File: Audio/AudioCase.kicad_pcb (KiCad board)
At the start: 2 copper layers, 271 x 112.8 mm, 87 parts, among them J10 AMP_AUX_IN, J11 AMP_AUX_OUT, J4 PWR_IN, J5 PWR_OUT, J6 AUX_IN, J7 V_IN, J8 AUX_OUT, J9 AMP_PWR, U3 NJM4558, U4 NJM4558

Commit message: Audio: Controll端子・リレー配線とPCB部品配置まで反映。
ControllにAmp向け2P端子10個とリレー周りの回路を更新し、AudioCaseへフットプリントを配置。EQ/Amp/Controllは回路図レイアウトに合わせて部品位置を調整（PowerModuleは配線済みのため未変更）。BP5293-50フットプリント修正と配置用スクリプトを追加。

Co-authored-by: Cursor <cursoragent@cursor.com>
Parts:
- removed C30: 0.1μF, Capacitor_THT:C_Rect_L7.2mm_W2.5mm_P5.00mm_FKS2_FKP2_MKS2_MKP2
- removed C31: 10μF, Capacitor_THT:CP_Radial_D5.0mm_P2.00mm
- removed C32, C33: 470μF, Capacitor_THT:CP_Radial_D16.0mm_P7.50mm
- removed F2: 1A, Resistor_THT:R_Axial_DIN0411_L9.9mm_D3.6mm_P12.70mm_Horizontal
- added A1: RaspberryPi_Pico, Module:RaspberryPi_Pico_Common_Unspecified, F.Cu at (100.8, 150.2)
- added C1: 47μF, Capacitor_THT:CP_Radial_D8.0mm_P3.50mm, F.Cu at (227.8, 39.2)
- added C2: 4.7μF, Capacitor_THT:CP_Radial_D5.0mm_P2.00mm, F.Cu at (256.0, 25.2)
- added C3: 4.7μF, Capacitor_THT:CP_Radial_D5.0mm_P2.00mm, F.Cu at (256.2, 45.7)
- added C4: 0.1μF, Capacitor_SMD:C_1206_3216Metric_Pad1.33x1.80mm_HandSolder, F.Cu at (256.0, 31.5)
- added F1: 1A, Resistor_THT:R_Axial_DIN0411_L9.9mm_D3.6mm_P12.70mm_Horizontal, F.Cu at (220.0, 33.4)
- added H13: MountingHole, MountingHole:MountingHole_3.2mm_M3, F.Cu at (21.2, 159.7)
- added H14: MountingHole, MountingHole:MountingHole_3.2mm_M3, F.Cu at (21.2, 167.7)
- added H15: MountingHole, MountingHole:MountingHole_3.2mm_M3, F.Cu at (21.2, 175.6)
- added H16: MountingHole, MountingHole:MountingHole_3.2mm_M3, F.Cu at (21.2, 183.6)
- added J12: AMP1_PWR, TerminalBlock_Phoenix:TerminalBlock_Phoenix_MKDS-1,5-2-5.08_1x02_P5.08mm_Horizontal, F.Cu at (60.8, 68.6)
- added J13: AMP1_PWR, TerminalBlock_Phoenix:TerminalBlock_Phoenix_MKDS-1,5-2-5.08_1x02_P5.08mm_Horizontal, F.Cu at (68.4, 119.2)
- added J14: AMP1_PWR, TerminalBlock_Phoenix:TerminalBlock_Phoenix_MKDS-1,5-2-5.08_1x02_P5.08mm_Horizontal, F.Cu at (68.9, 127.3)
- added J15: AMP1_LR, TerminalBlock_Phoenix:TerminalBlock_Phoenix_MKDS-1,5-2-5.08_1x02_P5.08mm_Horizontal, F.Cu at (80.3, 70.3)
- added J16: AMP2_PWR, TerminalBlock_Phoenix:TerminalBlock_Phoenix_MKDS-1,5-2-5.08_1x02_P5.08mm_Horizontal, F.Cu at (102.6, 68.6)
- added J17: AMP2_LR, TerminalBlock_Phoenix:TerminalBlock_Phoenix_MKDS-1,5-2-5.08_1x02_P5.08mm_Horizontal, F.Cu at (122.7, 70.3)
- added J18: AMP3_PWR, TerminalBlock_Phoenix:TerminalBlock_Phoenix_MKDS-1,5-2-5.08_1x02_P5.08mm_Horizontal, F.Cu at (142.3, 69.2)
- added J19: AMP4_PWR, TerminalBlock_Phoenix:TerminalBlock_Phoenix_MKDS-1,5-2-5.08_1x02_P5.08mm_Horizontal, F.Cu at (142.8, 85.0)
- added J20: AMP5_PWR, TerminalBlock_Phoenix:TerminalBlock_Phoenix_MKDS-1,5-2-5.08_1x02_P5.08mm_Horizontal, F.Cu at (143.9, 101.8)
- added J21: AMP3_PWR, TerminalBlock_Phoenix:TerminalBlock_Phoenix_MKDS-1,5-2-5.08_1x02_P5.08mm_Horizontal, F.Cu at (162.4, 70.8)
- added J22: AMP4_PWR, TerminalBlock_Phoenix:TerminalBlock_Phoenix_MKDS-1,5-2-5.08_1x02_P5.08mm_Horizontal, F.Cu at (163.5, 86.6)
- added J23: AMP5_PWR, TerminalBlock_Phoenix:TerminalBlock_Phoenix_MKDS-1,5-2-5.08_1x02_P5.08mm_Horizontal, F.Cu at (164.0, 103.4)
- added J24: OLED_PIN, TerminalBlock_Phoenix:TerminalBlock_Phoenix_MKDS-1,5-4-5.08_1x04_P5.08mm_Horizontal, F.Cu at (73.3, 98.0)
- added K1: AZ850P2-x, Relay_THT:Relay_DPDT_FRT5, F.Cu at (67.3, 72.5)
- added K10: AZ850P2-x, Relay_THT:Relay_DPDT_FRT5, F.Cu at (167.5, 113.8)
- added K2: AZ850P2-x, Relay_THT:Relay_DPDT_FRT5, F.Cu at (87.4, 74.1)
- added K3: AZ850P2-x, Relay_THT:Relay_DPDT_FRT5, F.Cu at (109.1, 72.5)
- added K4: AZ850P2-x, Relay_THT:Relay_DPDT_FRT5, F.Cu at (129.2, 74.1)
- added K5: AZ850P2-x, Relay_THT:Relay_DPDT_FRT5, F.Cu at (148.8, 73.0)
- added K6: AZ850P2-x, Relay_THT:Relay_DPDT_FRT5, F.Cu at (149.4, 88.8)
- added K7: AZ850P2-x, Relay_THT:Relay_DPDT_FRT5, F.Cu at (150.4, 105.6)
- added K8: AZ850P2-x, Relay_THT:Relay_DPDT_FRT5, F.Cu at (168.9, 74.6)
- added K9: AZ850P2-x, Relay_THT:Relay_DPDT_FRT5, F.Cu at (169.5, 90.4)
- added NT1: NetTie_2, NetTie:NetTie-2_THT_Pad1.0mm, F.Cu at (62.9, 121.4)
- added SW1: RotaryEncoder_Switch, Rotary_Encoder:RotaryEncoder_Alps_EC11E-Switch_Vertical_H20mm, F.Cu at (62.4, 104.0)
- added U1: MCW03, Library:MCW03-12D15_SIP7_THT, F.Cu at (225.9, 54.9)
- added U5: ULN2803A, Library:ULN2803A_DIP-18_W7.62mm, F.Cu at (124.4, 93.1)
- added U6: ULN2803A, Library:ULN2803A_DIP-18_W7.62mm, F.Cu at (124.9, 111.0)
- added U7: ULN2803A, Library:ULN2803A_DIP-18_W7.62mm, F.Cu at (124.9, 125.7)
- C10, C15: value 0.047μF -> 0.01uF; footprint Capacitor_THT:C_Rect_L7.2mm_W3.5mm_P5.00mm_FKS2_FKP2_MKS2_MKP2 -> Capacitor_THT:C_Rect_L7.2mm_W3.0mm_P5.00mm_FKS2_FKP2_MKS2_MKP2
- C11: value 0.01uF -> 0.047μF; footprint Capacitor_THT:C_Rect_L7.2mm_W3.0mm_P5.00mm_FKS2_FKP2_MKS2_MKP2 -> Capacitor_THT:C_Rect_L7.2mm_W3.5mm_P5.00mm_FKS2_FKP2_MKS2_MKP2
- C13: value 2200pF -> 0.01uF; footprint Capacitor_THT:C_Rect_L7.2mm_W4.5mm_P5.00mm_FKS2_FKP2_MKS2_MKP2 -> Capacitor_THT:C_Rect_L7.2mm_W3.0mm_P5.00mm_FKS2_FKP2_MKS2_MKP2
- C14, C17: value 0.01uF -> 2200pF; footprint Capacitor_THT:C_Rect_L7.2mm_W3.0mm_P5.00mm_FKS2_FKP2_MKS2_MKP2 -> Capacitor_THT:C_Rect_L7.2mm_W4.5mm_P5.00mm_FKS2_FKP2_MKS2_MKP2
- C16: value 0.047μF -> 2200pF; footprint Capacitor_THT:C_Rect_L7.2mm_W3.5mm_P5.00mm_FKS2_FKP2_MKS2_MKP2 -> Capacitor_THT:C_Rect_L7.2mm_W4.5mm_P5.00mm_FKS2_FKP2_MKS2_MKP2
- C18, C20, C21: value 2200pF -> 0.1μF; footprint Capacitor_THT:C_Rect_L7.2mm_W4.5mm_P5.00mm_FKS2_FKP2_MKS2_MKP2 -> Capacitor_SMD:C_1206_3216Metric_Pad1.33x1.80mm_HandSolder
- C19: value 0.01uF -> 0.1μF; footprint Capacitor_THT:C_Rect_L7.2mm_W3.0mm_P5.00mm_FKS2_FKP2_MKS2_MKP2 -> Capacitor_SMD:C_1206_3216Metric_Pad1.33x1.80mm_HandSolder
- C22, C23: footprint Capacitor_SMD:C_1206_3216Metric_Pad1.33x1.80mm_HandSolder -> Resistor_SMD:R_0603_1608Metric_Pad0.98x0.95mm_HandSolder
- C24, C26: footprint Capacitor_SMD:C_1206_3216Metric_Pad1.33x1.80mm_HandSolder -> Capacitor_THT:C_Rect_L7.2mm_W2.5mm_P5.00mm_FKS2_FKP2_MKS2_MKP2
- C25, C27: value 0.1μF -> 10μF; footprint Capacitor_SMD:C_1206_3216Metric_Pad1.33x1.80mm_HandSolder -> Capacitor_THT:CP_Radial_D5.0mm_P2.00mm
- C28: value 0.1μF -> 470μF; footprint Capacitor_THT:C_Rect_L7.2mm_W2.5mm_P5.00mm_FKS2_FKP2_MKS2_MKP2 -> Capacitor_THT:CP_Radial_D16.0mm_P7.50mm
- C29: value 10μF -> 470μF; footprint Capacitor_THT:CP_Radial_D5.0mm_P2.00mm -> Capacitor_THT:CP_Radial_D16.0mm_P7.50mm
- C5: value 47μF -> 0.1μF; footprint Capacitor_THT:CP_Radial_D8.0mm_P3.50mm -> Capacitor_SMD:C_1206_3216Metric_Pad1.33x1.80mm_HandSolder
- C6: value 4.7μF -> 0.047μF; footprint Capacitor_THT:CP_Radial_D5.0mm_P2.00mm -> Capacitor_THT:C_Rect_L7.2mm_W3.5mm_P5.00mm_FKS2_FKP2_MKS2_MKP2
- C7: value 4.7μF -> 0.01uF; footprint Capacitor_THT:CP_Radial_D5.0mm_P2.00mm -> Capacitor_THT:C_Rect_L7.2mm_W3.0mm_P5.00mm_FKS2_FKP2_MKS2_MKP2
- C8: value 0.1μF -> 0.047μF; footprint Capacitor_SMD:C_1206_3216Metric_Pad1.33x1.80mm_HandSolder -> Capacitor_THT:C_Rect_L7.2mm_W3.5mm_P5.00mm_FKS2_FKP2_MKS2_MKP2
- C9: value 0.1μF -> 2200pF; footprint Capacitor_SMD:C_1206_3216Metric_Pad1.33x1.80mm_HandSolder -> Capacitor_THT:C_Rect_L7.2mm_W4.5mm_P5.00mm_FKS2_FKP2_MKS2_MKP2
- R19, R20, R21, R22, R23, R24, R25, R26, R27, R28: footprint Resistor_SMD:R_1206_3216Metric_Pad1.30x1.75mm_HandSolder -> Resistor_SMD:R_0603_1608Metric_Pad0.98x0.95mm_HandSolder
- U2: value ~ -> NJM4558; footprint Library:MCW03-12D15_SIP7_THT -> Package_DIP:DIP-8_W7.62mm_Socket
- U4: value NJM4558 -> BP5293-50; footprint Package_DIP:DIP-8_W7.62mm_Socket -> BP5293_ROHM:BP5293-50_ROHM_SIP-3
- moved J9 263.2 mm to (265.7, 80.5), turned to 180 degrees
- moved C20 256.0 mm to (265.6, 94.0)
- moved H9 255.6 mm to (266.5, 141.8)
- moved H10 255.5 mm to (266.5, 146.4)
- moved H11 255.3 mm to (266.5, 151.1)
- moved H12 255.2 mm to (266.5, 155.8)
- moved C21 252.8 mm to (265.6, 108.0)
- moved C26 251.4 mm to (208.8, 148.5)
- moved C18 248.5 mm to (249.2, 94.0)
- moved C6 245.0 mm to (11.1, 22.7)
- moved C19 244.9 mm to (249.2, 108.0)
- moved C9 241.6 mm to (23.9, 105.7)
- moved C7 241.1 mm to (15.7, 65.9)
- moved C27 239.8 mm to (208.8, 156.7)
- moved C8 234.6 mm to (21.6, 22.7)
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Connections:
- AMP1 pad 4: /AmpModule/V-_IN -> /Controll/AMP_V-_OUT
- AMP1 pad 8: /AmpModule/V+_IN -> /Controll/AMP_V+_OUT
- C12 pad 1: Net-(C10-Pad2) -> Net-(C11-Pad2)
- C14 pad 1: Net-(C11-Pad2) -> Net-(C14-Pad1)
- C15 pad 1: Net-(C15-Pad1) -> Net-(C13-Pad2)
- C16 pad 1: Net-(C15-Pad2) -> Net-(C16-Pad1)
- C17 pad 1: Net-(C17-Pad1) -> Net-(C16-Pad2)
- C18 pad 1: Net-(C13-Pad2) -> /Controll/AMP_V+_IN
- C18 pad 2: Net-(C18-Pad2) -> GND
- C19 pad 1: Net-(C17-Pad2) -> GND
- C19 pad 2: Net-(C19-Pad2) -> /Controll/AMP_V-_IN
- C20 pad 1: Net-(C20-Pad1) -> /Controll/AMP_V+_IN
- C20 pad 2: Net-(C20-Pad2) -> GND
- C21 pad 1: Net-(C20-Pad2) -> GND
- C21 pad 2: Net-(C21-Pad2) -> /Controll/AMP_V-_IN
- C22 pad 1: /Controll/AMP_V+_IN -> GND
- C22 pad 2: GND -> /Controll/AMP_V+_OUT
- C23 pad 1: GND -> /Controll/AMP_V-_OUT
- C23 pad 2: /Controll/AMP_V-_IN -> GND
- C24 pad 1: /Controll/AMP_V+_IN -> Net-(AMP1A-+)
- C24 pad 2: GND -> /Controll/R_OUT
- C25 pad 1: GND -> Net-(AMP1A-+)
- C25 pad 2: /Controll/AMP_V-_IN -> /Controll/R_OUT
- C26 pad 1: GND -> Net-(AMP1B-+)
- C26 pad 2: /AmpModule/V+_IN -> /Controll/L_OUT
- C27 pad 1: /AmpModule/V-_IN -> Net-(AMP1B-+)
- C27 pad 2: GND -> /Controll/L_OUT
- C28 pad 1: Net-(AMP1A-+) -> Net-(C28-Pad1)
- C28 pad 2: /AmpModule/R_IN -> /AmpModule/R_OUT
- C29 pad 1: Net-(AMP1A-+) -> Net-(C29-Pad1)
- C29 pad 2: /AmpModule/R_IN -> /AmpModule/L_OUT
- C5 pad 1: Net-(U2-+Vin) -> GND
- C5 pad 2: /Controll/5VGND_CTRL -> /Controll/AMP_V-_IN
- C6 pad 1: /Controll/AMP_V+_IN -> Net-(C6-Pad1)
- C6 pad 2: GND -> Net-(C6-Pad2)
- C7 pad 1: GND -> Net-(C7-Pad1)
- C7 pad 2: /Controll/AMP_V-_IN -> Net-(C10-Pad1)
- C8 pad 1: /Controll/AMP_V+_IN -> Net-(C6-Pad2)
- C8 pad 2: GND -> Net-(C8-Pad2)
- C9 pad 1: GND -> Net-(C9-Pad1)
- C9 pad 2: /Controll/AMP_V-_IN -> Net-(C14-Pad1)
- J10 pad 1: /AmpModule/R_IN -> /Controll/R_OUT
- J10 pad 2: /AmpModule/L_IN -> /Controll/L_OUT
- J4 pad 1: /Controll/5VGND_CTRL -> /Controll/PD_GND_IN
- J4 pad 2: /PowerModule/+15_IN -> /Controll/+15_IN
- J9 pad 1: /AmpModule/V+_IN -> /Controll/AMP_V+_OUT
- J9 pad 3: /AmpModule/V-_IN -> /Controll/AMP_V-_OUT
- L1 pad 2: Net-(U2-+Vout) -> Net-(U1-+Vout)
- L2 pad 1: Net-(U2--Vout) -> Net-(U1--Vout)
- R1 pad 2: Net-(C10-Pad1) -> Net-(C6-Pad1)
- R10 pad 1: Net-(C15-Pad1) -> Net-(C11-Pad1)
- R11 pad 1: Net-(C17-Pad1) -> Net-(C13-Pad1)
- R12 pad 1: Net-(C20-Pad1) -> Net-(C16-Pad1)
- R15 pad 1: Net-(U4A--) -> Net-(U3A--)
- R16 pad 1: Net-(U4B--) -> Net-(U3B--)
- R17 pad 2: Net-(U4A--) -> Net-(U3A--)
- R18 pad 2: Net-(U4B--) -> Net-(U3B--)
- R19 pad 1: /AmpModule/R_IN -> /Controll/R_OUT
- R2 pad 2: Net-(C11-Pad1) -> Net-(C7-Pad1)
- R20 pad 1: /AmpModule/L_IN -> /Controll/L_OUT
- R27 pad 2: Net-(C32-Pad1) -> Net-(C28-Pad1)
- R28 pad 2: Net-(C33-Pad1) -> Net-(C29-Pad1)
- R3 pad 1: Net-(C10-Pad2) -> Net-(C6-Pad2)
- R4 pad 2: Net-(C13-Pad1) -> Net-(C9-Pad1)
- R5 pad 1: Net-(C16-Pad2) -> Net-(C12-Pad2)
- R6 pad 1: Net-(C11-Pad2) -> Net-(C10-Pad1)
- R7 pad 1: Net-(C19-Pad2) -> Net-(C15-Pad2)
- R8 pad 1: Net-(C13-Pad2) -> Net-(C14-Pad1)
- R9 pad 1: Net-(C21-Pad2) -> Net-(C17-Pad2)
- RV1 pad 1: Net-(C10-Pad1) -> Net-(C6-Pad1)
- RV1 pad 2: Net-(C10-Pad2) -> Net-(C6-Pad2)
- RV1 pad 3: Net-(C12-Pad2) -> Net-(C8-Pad2)
- RV1 pad 4: Net-(C16-Pad2) -> Net-(C12-Pad2)
- RV1 pad 5: Net-(C15-Pad2) -> Net-(C11-Pad2)
- RV1 pad 6: Net-(C15-Pad1) -> Net-(C11-Pad1)
- RV2 pad 1: Net-(C11-Pad1) -> Net-(C7-Pad1)
- RV2 pad 2: Net-(C11-Pad2) -> Net-(C10-Pad1)
- RV2 pad 3: Net-(C14-Pad2) -> Net-(C10-Pad2)
- RV2 pad 4: Net-(C19-Pad2) -> Net-(C15-Pad2)
- RV2 pad 5: Net-(C17-Pad2) -> Net-(C13-Pad2)
- RV2 pad 6: Net-(C17-Pad1) -> Net-(C13-Pad1)
- RV3 pad 1: Net-(C13-Pad1) -> Net-(C9-Pad1)
- RV3 pad 2: Net-(C13-Pad2) -> Net-(C14-Pad1)
- RV3 pad 3: Net-(C18-Pad2) -> Net-(C14-Pad2)
- RV3 pad 4: Net-(C21-Pad2) -> Net-(C17-Pad2)
- RV3 pad 5: Net-(C20-Pad2) -> Net-(C16-Pad2)
- RV3 pad 6: Net-(C20-Pad1) -> Net-(C16-Pad1)
- U2 pad 1: /Controll/5VGND_CTRL -> Net-(R13-Pad1)
- U2 pad 2: Net-(U2-+Vin) -> /EQModule/R BAX OUT
- U2 pad 3: unconnected-(U2-Remote_On/Off-Pad3) -> GND
- U2 pad 5: unconnected-(U2-NC-Pad5) -> GND
- U2 pad 6: Net-(U2-+Vout) -> /EQModule/L BAX OUT
- U2 pad 7: GND -> Net-(R14-Pad1)
- U2 pad 8: Net-(U2--Vout) -> /Controll/AMP_V+_IN
- U3 pad 1: Net-(R13-Pad1) -> /Controll/R_IN
- U3 pad 2: /EQModule/R BAX OUT -> Net-(U3A--)
- U3 pad 6: /EQModule/L BAX OUT -> Net-(U3B--)
- U3 pad 7: Net-(R14-Pad1) -> /Controll/L_IN
- U4 pad 1: /Controll/R_IN -> Net-(U4-VIN)
- U4 pad 2: Net-(U4A--) -> /Controll/CTRL_GND
- U4 pad 3: GND -> /Controll/5V_+
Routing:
- net Net-(U2-+Vin): track 37.9 -> 0.00 mm
- net /Controll/PD_GND_IN: track 0.00 -> 31.4 mm
- net /Controll/5VGND_CTRL: track 31.2 -> 0.00 mm
- net Net-(U1-+Vout): track 0.00 -> 30.8 mm
- net Net-(U2-+Vout): track 30.8 -> 0.00 mm
- net Net-(U1-+Vin): track 0.00 -> 26.6 mm
- net Net-(U2--Vout): track 17.6 -> 0.00 mm
- net Net-(U1--Vout): track 0.00 -> 14.1 mm
- net /PowerModule/+15_IN: track 11.0 -> 0.00 mm
- net /Controll/+15_IN: track 0.00 -> 9.99 mm
- net (no net): track 0.00 -> 3.50 mm
- net /Controll/AMP_V+_IN: track 55.2 -> 53.6 mm
- net /Controll/AMP_V-_IN: track 37.0 -> 36.4 mm
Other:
- board size 271 x 112.8 mm -> 277.5 x 115.3 mm

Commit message: Update audio KiCad project wiring.
Co-authored-by: Cursor <cursoragent@cursor.com>
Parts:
- added C30: 47μF, Capacitor_THT:CP_Radial_D8.0mm_P3.50mm, F.Cu at (194.3, 125.8)
- added C31: 0.1μF, Capacitor_THT:C_Disc_D5.0mm_W2.5mm_P2.50mm, F.Cu at (193.8, 133.4)
- added C32: 100μF, Capacitor_THT:CP_Radial_D6.3mm_P2.50mm, F.Cu at (195.3, 158.6)
- added C33: 0.1μF, Capacitor_THT:C_Disc_D5.0mm_W2.5mm_P2.50mm, F.Cu at (195.3, 151.8)
- added F2: 1A, Resistor_THT:R_Axial_DIN0411_L9.9mm_D3.6mm_P12.70mm_Horizontal, F.Cu at (186.2, 117.4)
- C19, C22, C23, R17, R19, R20, R21, R22, R23, R24: moved to B.Cu
- J13: value AMP1_PWR -> PD_IN
- J14: value AMP1_PWR -> AUDIO_IN
- J21: value AMP3_PWR -> AMP3_LR
- J22: value AMP4_PWR -> AMP4_LR
- J23: value AMP5_PWR -> AMP5_LR
- J24: footprint TerminalBlock_Phoenix:TerminalBlock_Phoenix_MKDS-1,5-4-5.08_1x04_P5.08mm_Horizontal -> Connector_PinHeader_2.54mm:PinHeader_1x04_P2.54mm_Vertical
- moved H7 197.4 mm to (168.2, 68.6)
- moved H6 184.5 mm to (168.2, 22.4)
- moved RV3 150.9 mm to (144.0, 65.8), turned to 90 degrees
- moved C19 149.4 mm to (118.2, 36.1)
- moved R17 140.9 mm to (146.5, 34.0)
- moved R15 139.7 mm to (133.7, 32.0), turned to 180 degrees
- moved C18 139.1 mm to (126.6, 28.5), turned to 90 degrees
- moved R4 137.7 mm to (138.5, 49.7), turned to -90 degrees
- moved NT1 137.2 mm to (199.5, 108.2), turned to -90 degrees
- moved R9 134.8 mm to (144.3, 49.0), turned to 90 degrees
- moved R8 133.7 mm to (155.5, 48.9), turned to 90 degrees
- moved C14 131.7 mm to (155.5, 53.8), turned to -90 degrees
- moved C21 129.4 mm to (156.0, 39.1), turned to 180 degrees
- moved J7 128.1 mm to (120.3, 22.3)
- moved SW1 127.4 mm to (120.7, 217.3), turned to 90 degrees
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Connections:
- net /EQModule/L BAX OUT renamed /EQModule/L_BAX_SUM
- net /EQModule/R BAX OUT renamed /EQModule/R_BAX_SUM
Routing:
- net /EQModule/L_IN: track 0.00 -> 83.4 mm
- net /EQModule/R_IN: track 0.00 -> 82.3 mm, vias 0 -> 3
- net /EQModule/R_BAX_SUM: track 0.00 -> 79.8 mm, vias 0 -> 6
- net /EQModule/L_BAX_SUM: track 0.00 -> 76.2 mm, vias 0 -> 6
- net /Controll/AMP_V-_IN: track 36.4 -> 102.4 mm
- net /Controll/AMP_V+_IN: track 53.6 -> 107.3 mm, vias 2 -> 3
- net /Controll/CTRL_GND: track 0.00 -> 53.7 mm, vias 0 -> 5
- net Net-(AMP1A-+): track 0.00 -> 36.5 mm
- net Net-(AMP1B-+): track 0.00 -> 35.7 mm
- net Net-(C14-Pad1): track 0.00 -> 34.7 mm
- net Net-(C10-Pad1): track 0.00 -> 34.2 mm, vias 0 -> 1
- net Net-(U4-VIN): track 0.00 -> 33.0 mm
- net Net-(C6-Pad2): track 0.00 -> 32.1 mm, vias 0 -> 1
- net /Controll/L_OUT: track 0.00 -> 27.3 mm
- net /Controll/AMP_V-_OUT: track 0.00 -> 23.2 mm
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- added copper zone on B.Cu, net /Controll/CTRL_GND
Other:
- board size 277.5 x 115.3 mm -> 262.1 x 203.6 mm

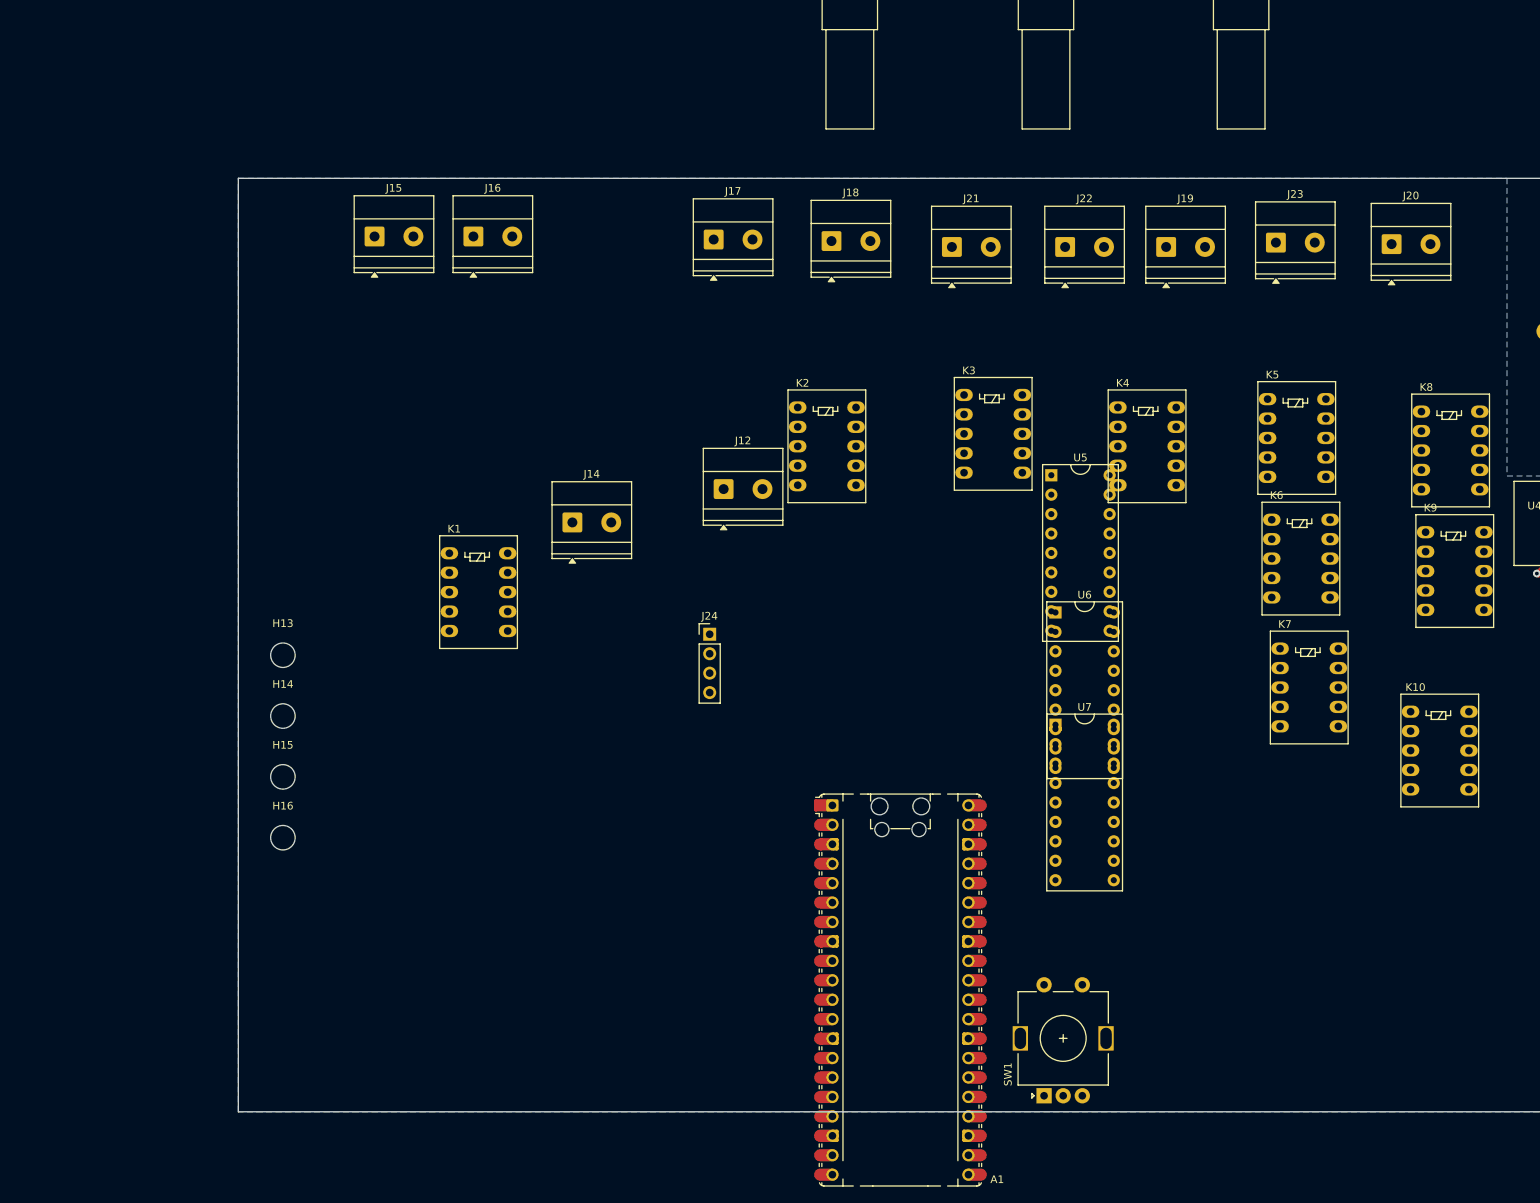
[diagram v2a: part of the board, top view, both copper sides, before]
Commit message: Update AudioCase PCB with new footprints and layout adjustments for components. Added mounting hole and resistor footprints, ensuring proper alignment with the circuit design. Co-authored-by: Cursor <cursoragent@cursor.com>
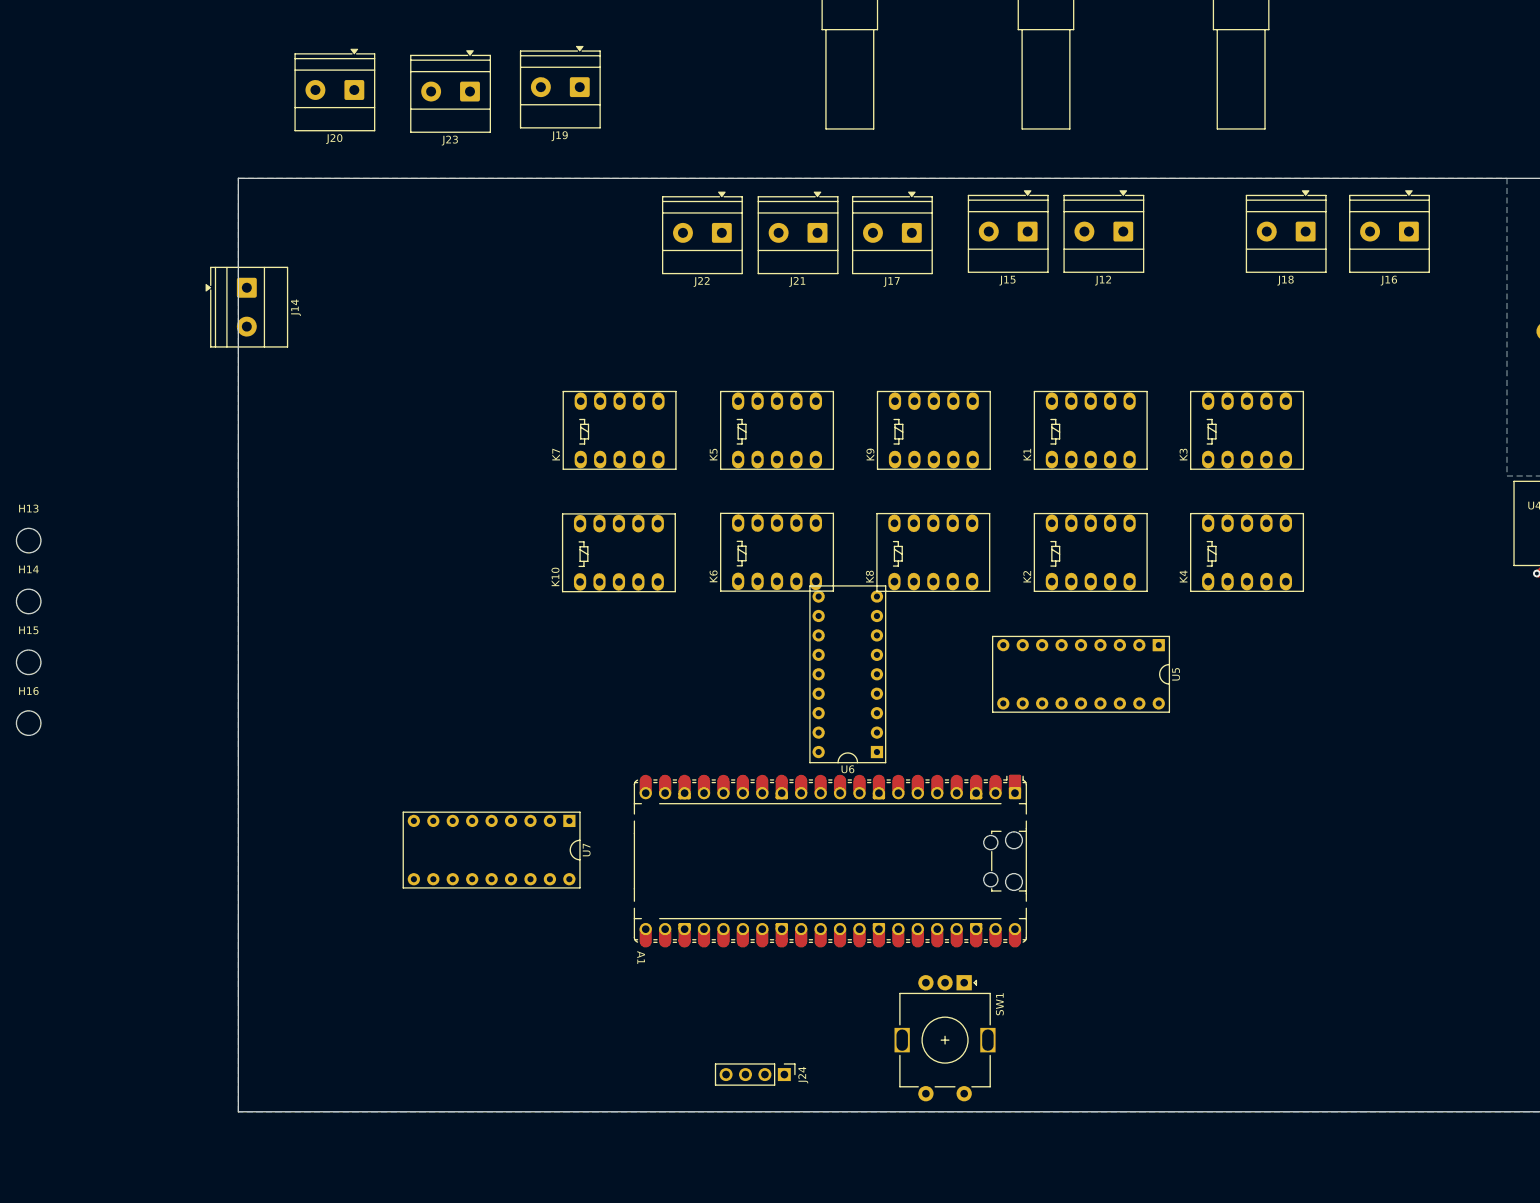
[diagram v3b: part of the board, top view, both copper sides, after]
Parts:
- moved J20 137.1 mm to (30.6, 85.9), turned to 180 degrees
- moved J16 122.3 mm to (168.4, 104.4), turned to 180 degrees
- moved K10 109.9 mm to (60.1, 150.2), turned to 90 degrees
- moved J23 107.2 mm to (45.7, 86.1), turned to 180 degrees
- moved K7 94.7 mm to (60.1, 134.2), turned to 90 degrees
- moved J15 85.4 mm to (118.6, 104.4), turned to 180 degrees
- moved K1 79.7 mm to (121.7, 134.2), turned to 90 degrees
- moved J19 79.4 mm to (60.0, 85.5), turned to 180 degrees
- moved U7 77.8 mm to (48.5, 185.2), turned to -90 degrees
- moved K8 72.4 mm to (101.1, 150.1), turned to 90 degrees
- moved K6 70.2 mm to (80.7, 150.1), turned to 90 degrees
- moved K9 70.0 mm to (101.2, 134.2), turned to 90 degrees
- moved K5 69.6 mm to (80.7, 134.2), turned to 90 degrees
- moved J12 62.1 mm to (131.1, 104.4), turned to 180 degrees
- moved J18 62.0 mm to (154.9, 104.4), turned to 180 degrees
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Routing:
- net /Controll/L_OUT: track 27.3 -> 28.2 mm
